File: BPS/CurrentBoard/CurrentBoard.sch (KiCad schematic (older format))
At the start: 1 part

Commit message: Finished basic connections. Still need to add DC-DC converter and connection for interrupts if needed.
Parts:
- added 100n (x2), 1u (x2): C, symbol Device:C
- added 100u: R, symbol Device:R
- added J?: Conn_01x04, symbol Connector_Generic:Conn_01x04
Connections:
- net labels added: +3.3V, GND
- wire segments 0 -> 34
- no-connect marks 0 -> 7
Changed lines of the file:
@@
 	1    0    0    -1
 $EndComp
+$Comp
+L Device:R 100u
+U 1 1 5F0E626E
+P 4950 3400
+F 0 "100u" V 4950 3300 50  0000 L CNN
+F 1 "R" V 4850 3400 50  0000 L CNN
+F 2 "" V 4880 3400 50  0001 C CNN
+F 3 "~" H 4950 3400 50  0001 C CNN
+	1    4950 3400
+	0    1    1    0
+$EndComp
+$Comp
+L Connector_Generic:Conn_01x04 J?
+U 1 1 5F0D0A13
+P 8100 4200
+F 0 "J?" H 8180 4192 50  0000 L CNN
+F 1 "Conn_01x04" H 8180 4101 50  0000 L CNN
+F 2 "" H 8100 4200 50  0001 C CNN
+F 3 "~" H 8100 4200 50  0001 C CNN
+	1    8100 4200
+	1    0    0    -1
+$EndComp
+NoConn ~ 6700 3500
+$Comp
+L Device:C 1u
+U 1 1 5F0D29CE
+P 4000 3850
+F 0 "1u" H 4115 3896 50  0000 L CNN
+F 1 "C" H 4115 3805 50  0000 L CNN
+F 2 "" H 4038 3700 50  0001 C CNN
+F 3 "~" H 4000 3850 50  0001 C CNN
+	1    4000 3850
+	1    0    0    -1
+$EndComp
+$Comp
+L power:GND #PWR?
+U 1 1 5F0CFF58
+P 4000 4000
+F 0 "#PWR?" H 4000 3750 50  0001 C CNN
+F 1 "GND" H 4050 3850 50  0000 R CNN
+F 2 "" H 4000 4000 50  0001 C CNN
+F 3 "" H 4000 4000 50  0001 C CNN
+	1    4000 4000
+	1    0    0    -1
+$EndComp
+$Comp
+L power:+3.3V #PWR?
+U 1 1 5F0CF90D
+P 4000 3700
+F 0 "#PWR?" H 4000 3550 50  0001 C CNN
+F 1 "+3.3V" H 3900 3850 50  0000 L CNN
+F 2 "" H 4000 3700 50  0001 C CNN
+F 3 "" H 4000 3700 50  0001 C CNN
+	1    4000 3700
+	1    0    0    -1
+$EndComp
+$Comp
+L Device:C 1u
+U 1 1 5F0D5530
+P 7150 3850
+F 0 "1u" H 7035 3896 50  0000 R CNN
+F 1 "C" H 7035 3805 50  0000 R CNN
+F 2 "" H 7188 3700 50  0001 C CNN
+F 3 "~" H 7150 3850 50  0001 C CNN
+	1    7150 3850
+	-1   0    0    -1
+$EndComp
+$Comp
+L power:GND #PWR?
+U 1 1 5F0D5536
+P 7150 4000
+F 0 "#PWR?" H 7150 3750 50  0001 C CNN
+F 1 "GND" H 7200 3850 50  0000 R CNN
+F 2 "" H 7150 4000 50  0001 C CNN
+F 3 "" H 7150 4000 50  0001 C CNN
+	1    7150 4000
+	-1   0    0    -1
+$EndComp
+$Comp
+L power:+3.3V #PWR?
+U 1 1 5F0D553C
+P 7150 3700
+F 0 "#PWR?" H 7150 3550 50  0001 C CNN
+F 1 "+3.3V" H 7050 3850 50  0000 L CNN
+F 2 "" H 7150 3700 50  0001 C CNN
+F 3 "" H 7150 3700 50  0001 C CNN
+	1    7150 3700
+	-1   0    0    -1
+$EndComp
+Wire Wire Line
+	6700 4300 6700 4450
+Wire Wire Line
+	6700 4450 7900 4450
+Wire Wire Line
+	7900 4450 7900 4400
+Wire Wire Line
+	6700 4200 6750 4200
+Wire Wire Line
+	6750 4200 6750 4300
+Wire Wire Line
+	6750 4300 7900 4300
+Wire Wire Line
+	6700 4100 6800 4100
+Wire Wire Line
+	6800 4100 6800 4200
+Wire Wire Line
+	6800 4200 7900 4200
+Wire Wire Line
+	6700 4000 7150 4000
+Connection ~ 7150 4000
+Wire Wire Line
+	6700 3900 6850 3900
+Wire Wire Line
+	6850 3900 6850 3700
+Wire Wire Line
+	6850 3700 7150 3700
+Connection ~ 7150 3700
+Wire Wire Line
+	6700 3600 6950 3600
+Wire Wire Line
+	6950 3600 6950 3500
+Wire Wire Line
+	6950 3500 7350 3500
+Wire Wire Line
+	7350 3500 7350 4100
+Wire Wire Line
+	7350 4100 7900 4100
+$Comp
+L Device:C 100n
+U 1 1 5F0DDF8B
+P 4650 3600
+F 0 "100n" V 4500 3500 50  0000 C CNN
+F 1 "C" V 4600 3450 50  0000 C CNN
+F 2 "" H 4688 3450 50  0001 C CNN
+F 3 "~" H 4650 3600 50  0001 C CNN
+	1    4650 3600
+	0    1    1    0
+$EndComp
+$Comp
+L power:GND #PWR?
+U 1 1 5F0DE420
+P 4500 3600
+F 0 "#PWR?" H 4500 3350 50  0001 C CNN
+F 1 "GND" V 4505 3472 50  0000 R CNN
+F 2 "" H 4500 3600 50  0001 C CNN
+F 3 "" H 4500 3600 50  0001 C CNN
+	1    4500 3600
+	0    1    1    0
+$EndComp
+$Comp
+L Device:C 100n
+U 1 1 5F0DEB81
+P 4900 3800
+F 0 "100n" V 4750 3700 50  0000 C CNN
+F 1 "C" V 4850 3650 50  0000 C CNN
+F 2 "" H 4938 3650 50  0001 C CNN
+F 3 "~" H 4900 3800 50  0001 C CNN
+	1    4900 3800
+	0    1    1    0
+$EndComp
+$Comp
+L power:GND #PWR?
+U 1 1 5F0DEB87
+P 4750 3800
+F 0 "#PWR?" H 4750 3550 50  0001 C CNN
+F 1 "GND" V 4755 3672 50  0000 R CNN
+F 2 "" H 4750 3800 50  0001 C CNN
+F 3 "" H 4750 3800 50  0001 C CNN
+	1    4750 3800
+	0    1    1    0
+$EndComp
+Wire Wire Line
+	5200 3500 4800 3500
+Wire Wire Line
+	4800 3500 4800 3400
+Wire Wire Line
+	5200 3600 4800 3600
+Wire Wire Line
+	5200 3700 5050 3700
+Wire Wire Line
+	5050 3700 5050 3800
+Wire Wire Line
+	5200 3800 5100 3800
+Wire Wire Line
+	5100 3800 5100 3900
+Wire Wire Line
+	5100 3900 4250 3900
+Wire Wire Line
+	4250 3900 4250 3700
+Wire Wire Line
+	4250 3700 4000 3700
+Connection ~ 4000 3700
+Wire Wire Line
+	5200 3900 5150 3900
+Wire Wire Line
+	5150 3900 5150 3950
+Wire Wire Line
+	5150 3950 4050 3950
+Wire Wire Line
+	4050 3950 4050 4000
+Wire Wire Line
+	4050 4000 4000 4000
+Connection ~ 4000 4000
+Wire Wire Line
+	5200 3400 5100 3400
+NoConn ~ 5200 4000
+NoConn ~ 5200 4100
+NoConn ~ 5200 4200
+NoConn ~ 5200 4300
+NoConn ~ 6700 3700
+NoConn ~ 6700 3800
 $EndSCHEMATC

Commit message: Completes schematic of current board
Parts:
- removed 100n (x2), 1u (x2): C, symbol Device:C
- removed 100u: R, symbol Device:R
- removed IC?: AS8510-ASSM, SOP65P780X200-20N, symbol utsvt-current:AS8510-ASSM
- added C1: 4.7u, Capacitor_SMD:C_0805_2012Metric, symbol Device:C
- added C10, C9: 0.1u, Capacitor_SMD:C_0805_2012Metric, symbol Device:C
- added C2, C3: 100n, Capacitor_SMD:C_0805_2012Metric, symbol Device:C
- added C4, C6: 10u, Capacitor_SMD:C_0805_2012Metric, symbol Device:C
- added C5: 470p, Capacitor_SMD:C_0805_2012Metric, symbol Device:C
- added C7, C8: 1u, Capacitor_SMD:C_0805_2012Metric, symbol Device:C
- added D1: PowerOn, LED_SMD:LED_0805_2012Metric, symbol Device:LED_ALT
- added H1, H2, H3, H4: MountingHole, MountingHole:MountingHole_3mm, symbol Mechanical:MountingHole
- added J1: ShuntConn, Connector_Molex:Molex_Micro-Fit_3.0_43650-0415_1x04_P3.00mm_Vertical, symbol Connector_Generic:Conn_01x04
- added L1: 10uH, UTSVT_BPS:SRF0905A, symbol utsvt-bps:SRF0905-100Y
- added R1: 1k, Resistor_SMD:R_0805_2012Metric, symbol Device:R
- added R2: 10k, Resistor_SMD:R_0805_2012Metric, symbol Device:R
- added R3: 1.5k, Resistor_SMD:R_0805_2012Metric, symbol Device:R
- added R4: 120, Resistor_SMD:R_0805_2012Metric, symbol Device:R
- added R5: 806, Resistor_SMD:R_0805_2012Metric, symbol Device:R
- added R6: 1.21k, Resistor_SMD:R_0805_2012Metric, symbol Device:R
- added TP1: +12V_TP, TestPoint:TestPoint_Keystone_5005-5009_Compact, symbol Connector:TestPoint
- added TP2: GNDPWR_TP, TestPoint:TestPoint_Keystone_5005-5009_Compact, symbol Connector:TestPoint
- added TP3: +3.3V_TP, TestPoint:TestPoint_Keystone_5005-5009_Compact, symbol Connector:TestPoint
- added TP4: +5V_TP, TestPoint:TestPoint_Keystone_5005-5009_Compact, symbol Connector:TestPoint
- added TP5: GND_TP, TestPoint:TestPoint_Keystone_5005-5009_Compact, symbol Connector:TestPoint
- added U1: AS8510-ASSM, UTSVT_ICs:AS8510-ASSM, symbol AS8510-ASSM:AS8510-ASSM
- added U2: RI3-1205S, UTSVT_ICs:RI3_DC_Converter, symbol utsvt-power-regulators:RI3-1205S
- added U3: NCP1117-3.3_SOT223, Package_TO_SOT_SMD:SOT-223-3_TabPin2, symbol Regulator_Linear:NCP1117-3.3_SOT223
- added U4: LTC6820, Package_SO:MSOP-16_3x4mm_P0.5mm, symbol utsvt-bps:LTC6820
- added U5: HX1188FNL, UTSVT_BPS:HXXXX, symbol utsvt-bps:HX1188FNL
- J2: renamed from J?; value Conn_01x04 -> LeaderConn; footprint (none) -> Connector_Molex:Molex_Micro-Fit_3.0_43650-0415_1x04_P3.00mm_Vertical
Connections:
- net labels added: +12V, +5V, CS, ETS, GNDPWR, IM, IP, MISO, MOSI, RSHH, RSHL, SCK
- wire segments 34 -> 125
- no-connect marks 7 -> 13
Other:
- note added: "Current Sensor"
- note added: "Current shunt resistor (100u ohms) and thermistor (PT1000) will\nbe placed on a separate PCB located closer to the battery."
- note added: "Isolated SPI"
- note added: "Mounting Holes"
- note added: "Power"
- note added: "Temp co = 0\nConstant"
- moved on the sheet: J2

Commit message: Adds AS8510 into utsvt-bps.lib
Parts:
- U1: symbol AS8510-ASSM:AS8510-ASSM -> utsvt-bps:AS8510-ASSM
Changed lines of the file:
@@
 $EndComp
 $Comp
-L AS8510-ASSM:AS8510-ASSM U1
+L utsvt-bps:AS8510-ASSM U1
 U 1 1 5F15149C
 P 3150 5400

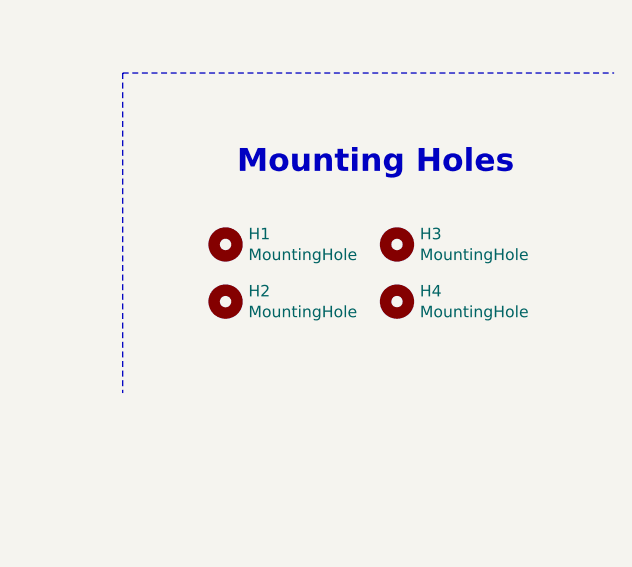
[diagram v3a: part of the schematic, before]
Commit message: Edits name of mounting holes to standardized M3 screw size
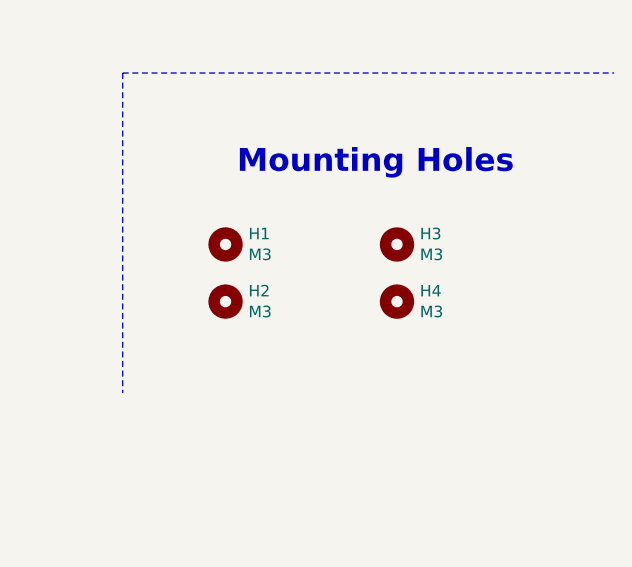
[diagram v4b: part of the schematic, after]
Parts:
- H1, H2, H3, H4: value MountingHole -> M3
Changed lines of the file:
@@
 P 10250 5900
 F 0 "H3" H 10350 5946 50  0000 L CNN
-F 1 "MountingHole" H 10350 5855 50  0000 L CNN
+F 1 "M3" H 10350 5855 50  0000 L CNN
 F 2 "MountingHole:MountingHole_3mm" H 10250 5900 50  0001 C CNN
 F 3 "~" H 10250 5900 50  0001 C CNN
@@
 P 10250 6150
 F 0 "H4" H 10350 6196 50  0000 L CNN
-F 1 "MountingHole" H 10350 6105 50  0000 L CNN
+F 1 "M3" H 10350 6105 50  0000 L CNN
 F 2 "MountingHole:MountingHole_3mm" H 10250 6150 50  0001 C CNN
 F 3 "~" H 10250 6150 50  0001 C CNN
@@
 P 9500 5900
 F 0 "H1" H 9600 5946 50  0000 L CNN
-F 1 "MountingHole" H 9600 5855 50  0000 L CNN
+F 1 "M3" H 9600 5855 50  0000 L CNN
 F 2 "MountingHole:MountingHole_3mm" H 9500 5900 50  0001 C CNN
 F 3 "~" H 9500 5900 50  0001 C CNN
@@
 P 9500 6150
 F 0 "H2" H 9600 6196 50  0000 L CNN
-F 1 "MountingHole" H 9600 6105 50  0000 L CNN
+F 1 "M3" H 9600 6105 50  0000 L CNN
 F 2 "MountingHole:MountingHole_3mm" H 9500 6150 50  0001 C CNN
 F 3 "~" H 9500 6150 50  0001 C CNN

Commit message: Updates footprint for 470pF capacitor
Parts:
- C5: footprint Capacitor_SMD:C_0805_2012Metric -> Capacitor_SMD:C_2220_5650Metric; Rating (none) -> 4kV
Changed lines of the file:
@@
 F 0 "C5" V 3398 1600 50  0000 C CNN
 F 1 "470p" V 3489 1600 50  0000 C CNN
-F 2 "Capacitor_SMD:C_0805_2012Metric" H 3688 1450 50  0001 C CNN
+F 2 "Capacitor_SMD:C_2220_5650Metric" H 3688 1450 50  0001 C CNN
 F 3 "~" H 3650 1600 50  0001 C CNN
+F 4 "4kV" V 3650 1600 50  0001 C CNN "Rating"
 	1    3650 1600
 	0    1    1    0

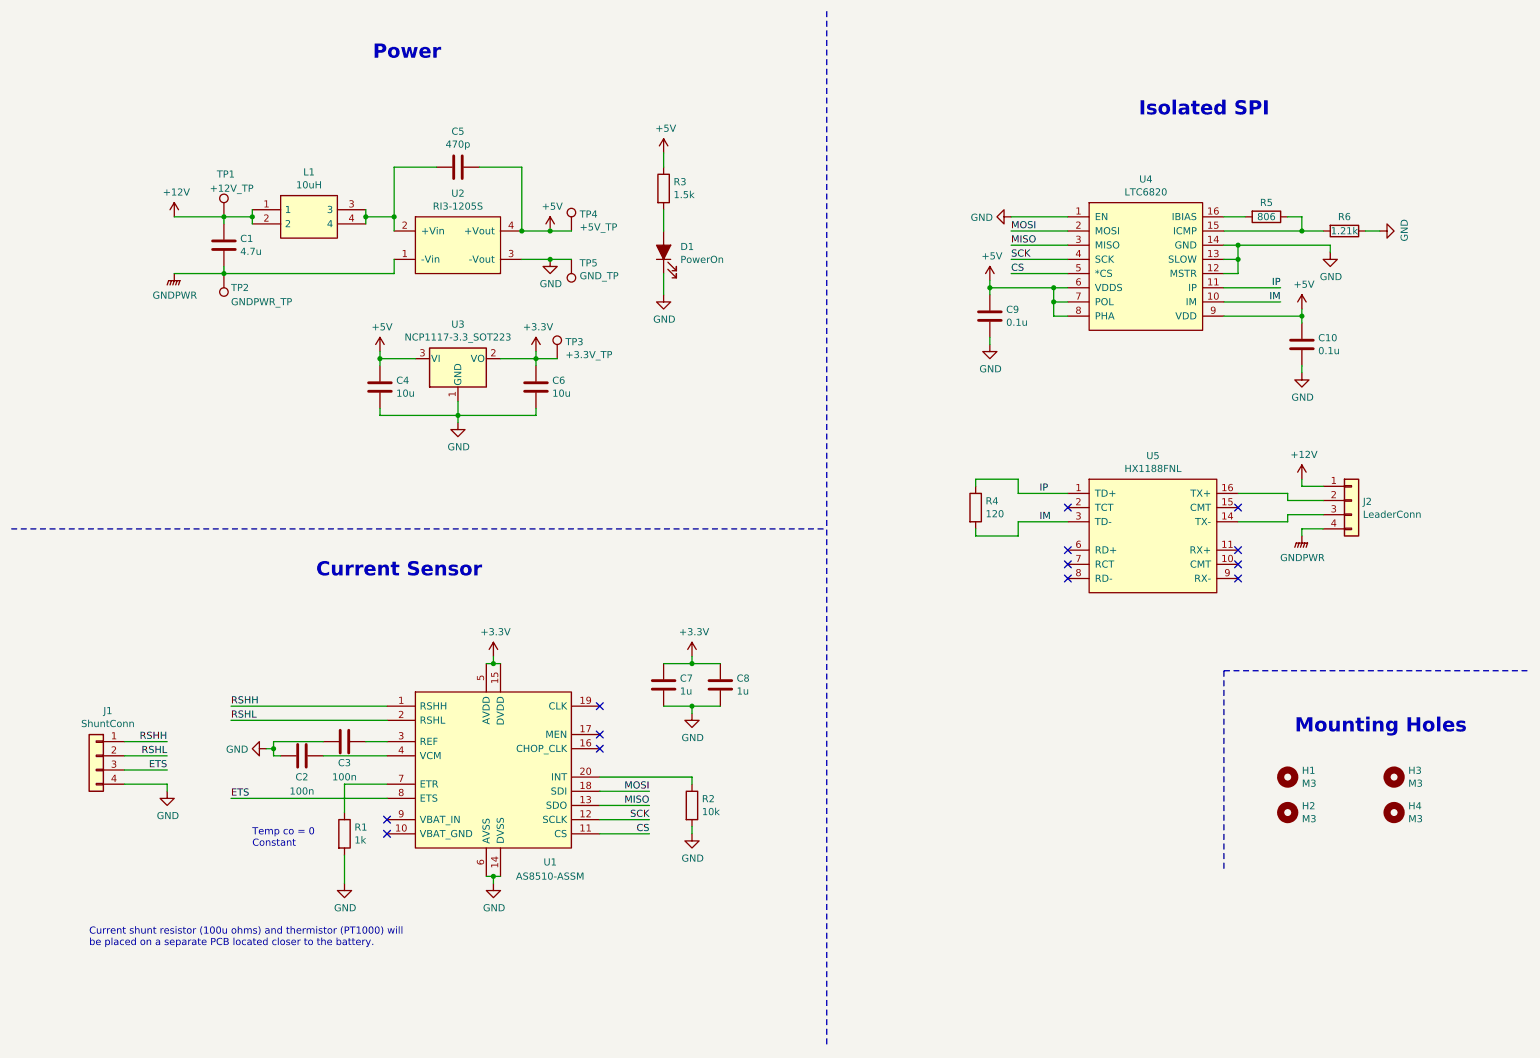
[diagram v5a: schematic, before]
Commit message: Completes current board schematic and starts PCB
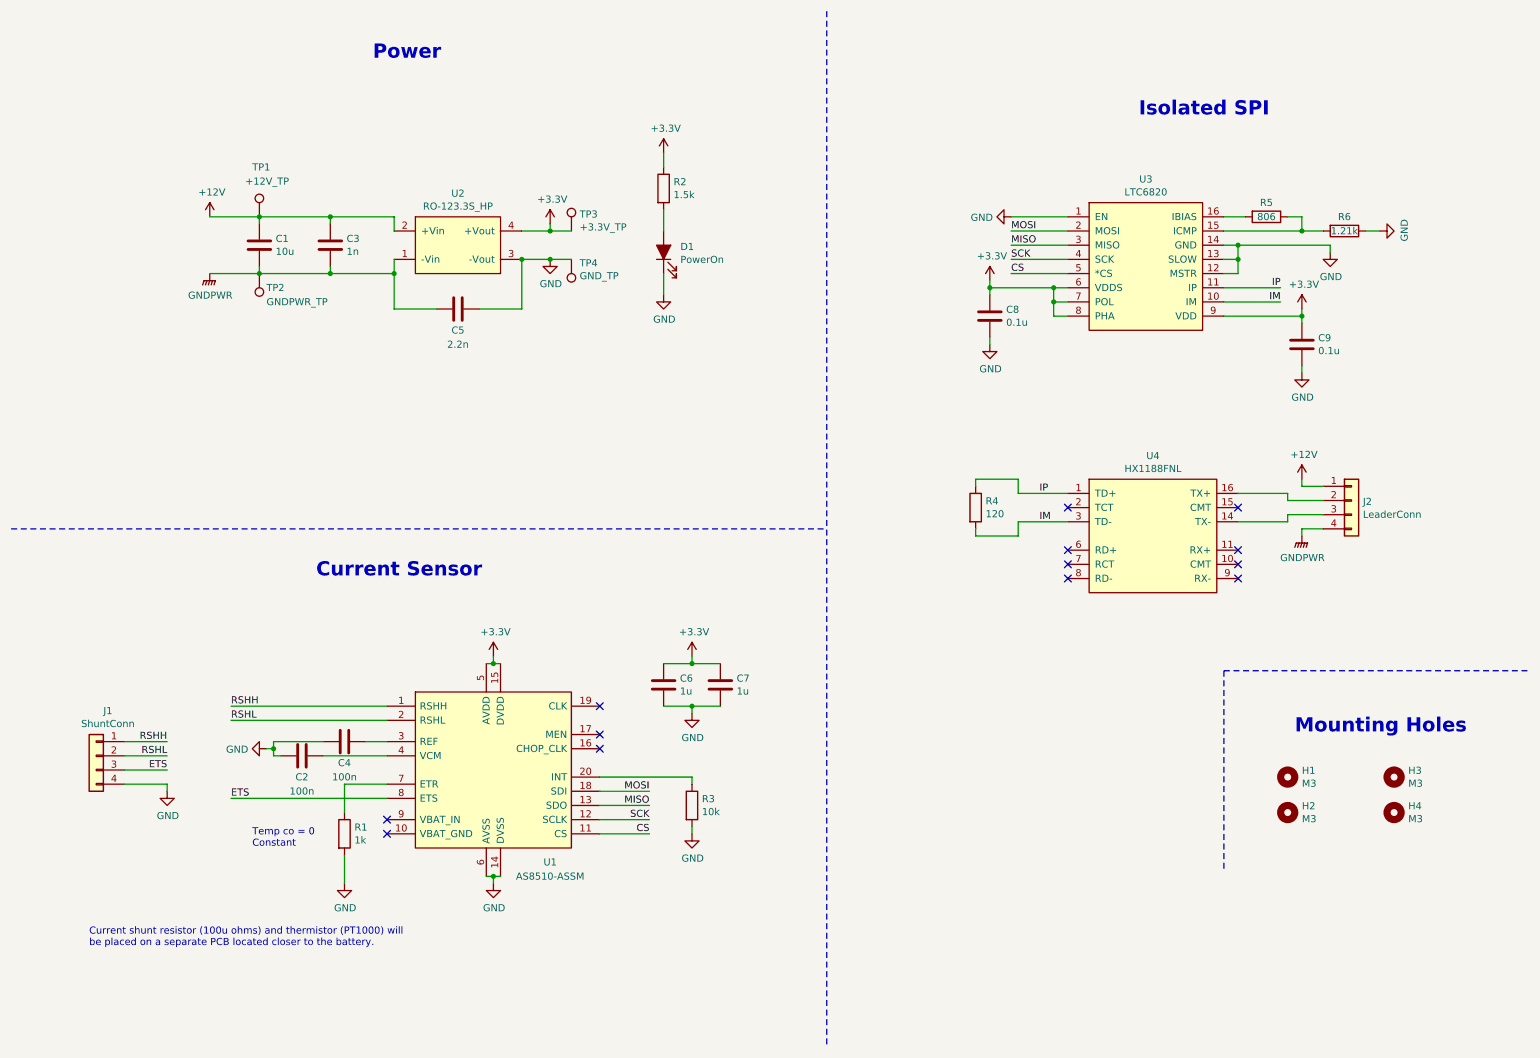
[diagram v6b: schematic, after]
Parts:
- removed C4, C6: 10u, Capacitor_SMD:C_0805_2012Metric, symbol Device:C
- removed L1: 10uH, UTSVT_BPS:SRF0905A, symbol utsvt-bps:SRF0905-100Y
- removed TP4: +5V_TP, TestPoint:TestPoint_Keystone_5005-5009_Compact, symbol Connector:TestPoint
- removed U2: RI3-1205S, UTSVT_ICs:RI3_DC_Converter, symbol utsvt-power-regulators:RI3-1205S
- removed U3: NCP1117-3.3_SOT223, Package_TO_SOT_SMD:SOT-223-3_TabPin2, symbol Regulator_Linear:NCP1117-3.3_SOT223
- added C3: 1n, Capacitor_SMD:C_0805_2012Metric, symbol Device:C
- added U2: RO-123.3S_HP, UTSVT_ICs:RI3_DC_Converter, symbol utsvt-power-regulators:RO-123.3S_HP
- C1: value 4.7u -> 10u; footprint Capacitor_SMD:C_0805_2012Metric -> UTSVT_Passive:C_2220_5750Metrix
- C5: value 470p -> 2.2n; footprint Capacitor_SMD:C_2220_5650Metric -> Capacitor_SMD:C_0805_2012Metric; Rating 4kV -> (none)
- renumbered C3 to C4, C7 to C6, C8 to C7, C9 to C8, C10 to C9, R3 to R2, R2 to R3, TP5 to TP4, U4 to U3, U5 to U4
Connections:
- net +12V: now also C3.1, U2.2 (+Vin)
- net +3V3: now also C8.1, C9.1, R2.1, U3.6 (VDDS), U3.7 (POL), U3.8 (PHA), U3.9 (VDD), U2.4 (+Vout)
- net GND: now also C5.2, U2.3 (-Vout)
- net GNDPWR: now also C5.1, C3.2, U2.1 (-Vin)
- removed net +5V: C5.1, C8.1, C9.1, R2.1, U3.6 (VDDS), U3.7 (POL), U3.8 (PHA), U3.9 (VDD)
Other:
- moved on the sheet: C1, TP1, TP2, TP3

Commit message: Finishes PCB layout of current board
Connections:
- net ETS: now also J1.1 (Pin_1); no longer J1.3 (Pin_3)
- net RSHH: now also J1.3 (Pin_3); no longer J1.1 (Pin_1)
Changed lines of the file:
@@
 	1    0    0    -1
 $EndComp
-Text Label 1600 5650 2    50   ~ 0
+Text Label 1600 5850 2    50   ~ 0
 RSHH
 Text Label 1600 5750 2    50   ~ 0
 RSHL
-Text Label 1600 5850 2    50   ~ 0
+Text Label 1600 5650 2    50   ~ 0
 ETS
 $Comp

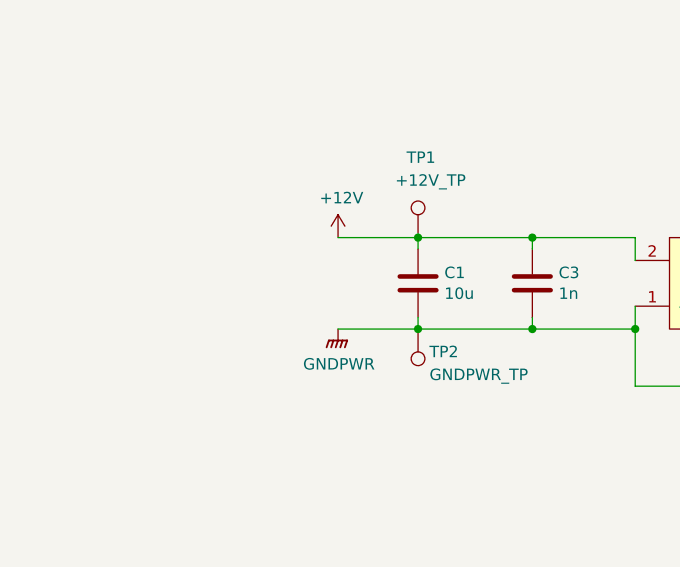
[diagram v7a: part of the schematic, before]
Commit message: Edits LTC6820 symbol, generates netlist, and fixes schematic errors
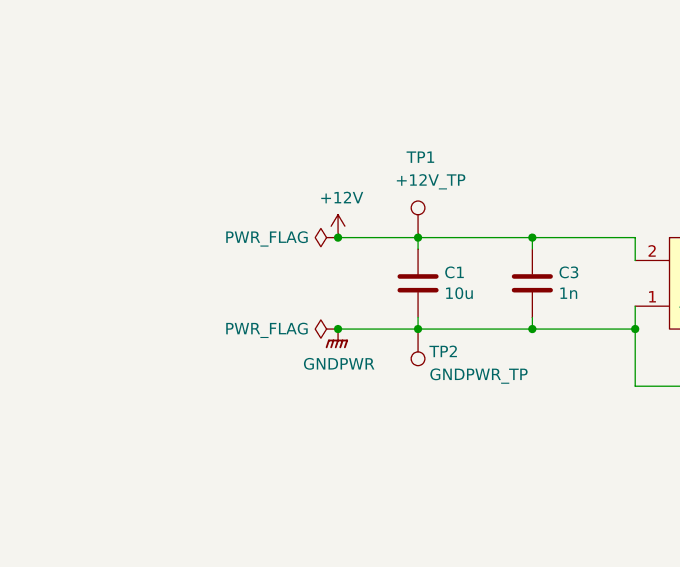
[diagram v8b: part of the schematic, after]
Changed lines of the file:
@@
 	3200 2350 3200 2250
 Wire Wire Line
-	5100 1500 5100 1600
-Wire Wire Line
 	5100 1900 5100 2050
-Wire Wire Line
-	5100 2350 5100 2500
 $Comp
 L power:+3.3V #PWR08
@@
 	1    0    0    -1
 $EndComp
+$Comp
+L power:PWR_FLAG #FLG0101
+U 1 1 5F26B04E
+P 1900 1950
+F 0 "#FLG0101" H 1900 2025 50  0001 C CNN
+F 1 "PWR_FLAG" V 1900 2077 50  0000 L CNN
+F 2 "" H 1900 1950 50  0001 C CNN
+F 3 "~" H 1900 1950 50  0001 C CNN
+	1    1900 1950
+	0    -1   -1   0
+$EndComp
+Connection ~ 1900 1950
+$Comp
+L power:PWR_FLAG #FLG0102
+U 1 1 5F26B529
+P 1900 2350
+F 0 "#FLG0102" H 1900 2425 50  0001 C CNN
+F 1 "PWR_FLAG" V 1900 2477 50  0000 L CNN
+F 2 "" H 1900 2350 50  0001 C CNN
+F 3 "~" H 1900 2350 50  0001 C CNN
+	1    1900 2350
+	0    -1   -1   0
+$EndComp
+Connection ~ 1900 2350
+Wire Wire Line
+	5100 2350 5100 2500
+Wire Wire Line
+	5100 1500 5100 1600
 $EndSCHEMATC
